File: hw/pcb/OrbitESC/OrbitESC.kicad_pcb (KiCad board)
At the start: 2 copper layers, 30 parts, among them J3 TermA, J4 TermB, J5 TermC, Q1 MCAC80N10Y, Q2 MCAC80N10Y, Q3 MCAC80N10Y, Q4 MCAC80N10Y, Q5 MCAC80N10Y, Q6 MCAC80N10Y, U1 MCP2551-I-SN, U2 AT25SF081-SSHD-X, U4 STM32F446ZCHx

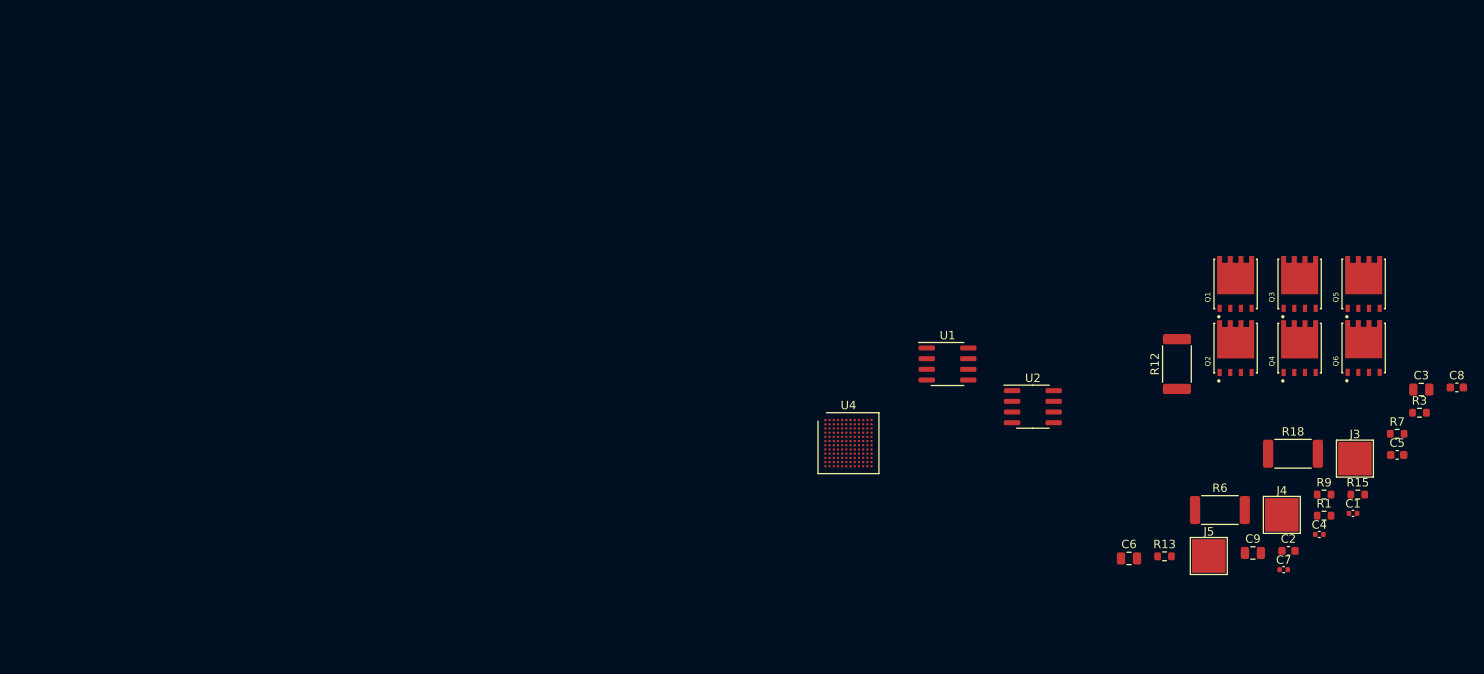
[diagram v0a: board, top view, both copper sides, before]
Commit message: Add power stage components
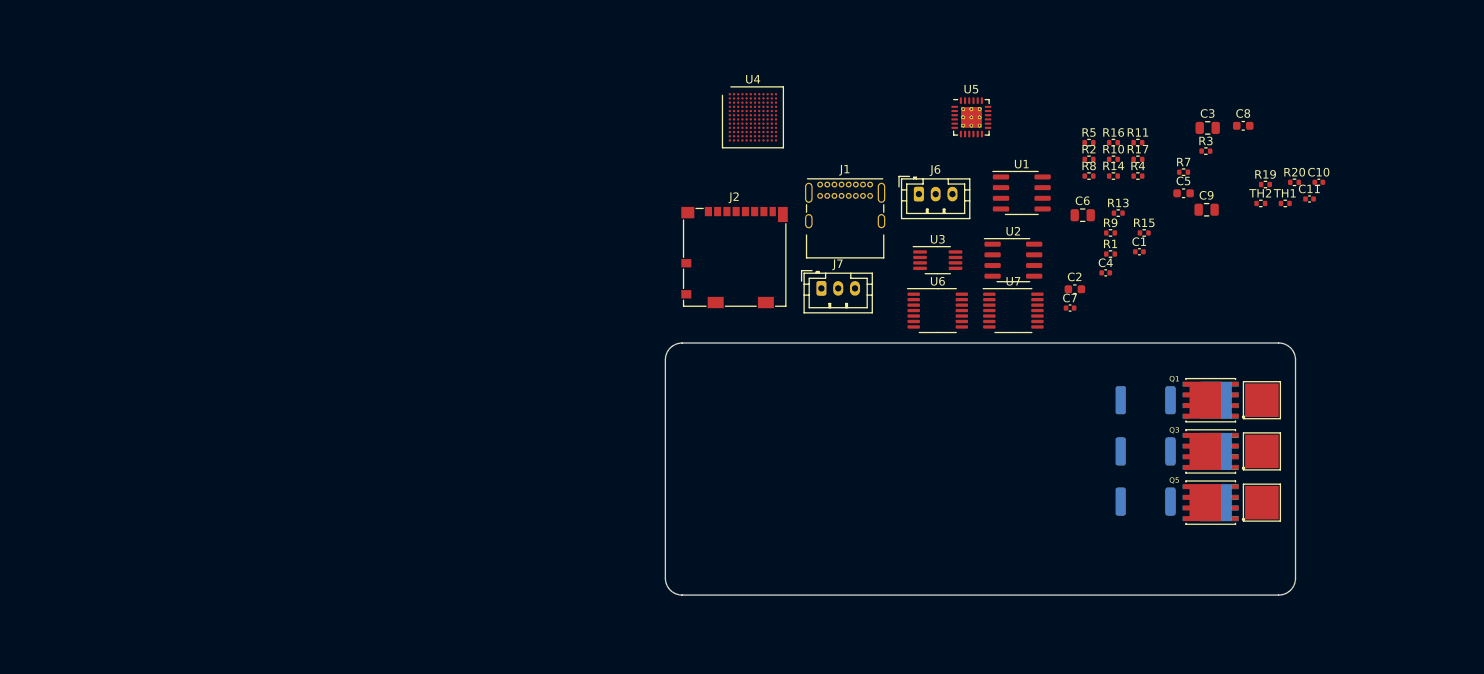
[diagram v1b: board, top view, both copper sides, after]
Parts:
- added C10: 1uF, Capacitor_SMD:C_0402_1005Metric, F.Cu at (181.3, 64.7)
- added C11: 1uF, Capacitor_SMD:C_0402_1005Metric, F.Cu at (180.2, 66.7)
- added J1: USB_C_Receptacle_USB2.0, Connector_USB:USB_C_Receptacle_GCT_USB4085, F.Cu at (122.0, 65.0)
- added J2: Micro_SD_Card_Det, Connector_Card:microSD_HC_Molex_104031-0811, F.Cu at (111.8, 73.7)
- added J6: CAN1, Connector_JST:JST_PH_B3B-PH-K_1x03_P2.00mm_Vertical, F.Cu at (133.8, 66.1)
- added J7: Serial1, Connector_JST:JST_PH_B3B-PH-K_1x03_P2.00mm_Vertical, F.Cu at (122.2, 77.4)
- added R10: 10, Resistor_SMD:R_0402_1005Metric, F.Cu at (156.9, 62.0)
- added R11: 39k, Resistor_SMD:R_0402_1005Metric, F.Cu at (159.8, 60.0)
- added R14: 10, Resistor_SMD:R_0402_1005Metric, F.Cu at (156.9, 64.0)
- added R16: 10, Resistor_SMD:R_0402_1005Metric, F.Cu at (156.9, 60.0)
- added R17: 39k, Resistor_SMD:R_0402_1005Metric, F.Cu at (159.8, 62.0)
- added R19: 1k, Resistor_SMD:R_0402_1005Metric, F.Cu at (175.0, 65.0)
- added R2: 10, Resistor_SMD:R_0402_1005Metric, F.Cu at (154.0, 62.0)
- added R20: 10k, Resistor_SMD:R_0402_1005Metric, F.Cu at (178.5, 64.7)
- added R4: 10, Resistor_SMD:R_0402_1005Metric, F.Cu at (159.8, 64.0)
- added R5: 39k, Resistor_SMD:R_0402_1005Metric, F.Cu at (154.0, 60.0)
- added R8: 10, Resistor_SMD:R_0402_1005Metric, F.Cu at (154.0, 64.0)
- added TH1: 10k NTC, Resistor_SMD:R_0402_1005Metric, F.Cu at (177.4, 67.2)
- added TH2: 10k NTC, Resistor_SMD:R_0402_1005Metric, F.Cu at (174.4, 67.2)
- added U3: 24LC128, Package_SO:MSOP-8_3x3mm_P0.65mm, F.Cu at (136.0, 74.0)
- added U5: DRV8300DRGER, Package_DFN_QFN:VQFN-24-1EP_4x4mm_P0.5mm_EP2.45x2.45mm_ThermalVias, F.Cu at (140.0, 57.0)
- added U6: TSV994, Package_SO:TSSOP-14_4.4x5mm_P0.65mm, F.Cu at (136.0, 80.0)
- added U7: TSV994, Package_SO:TSSOP-14_4.4x5mm_P0.65mm, F.Cu at (145.0, 80.0)
- Q2, Q4, Q6, R12, R18, R6: moved to B.Cu
- R1, R13: value 4.99k -> 1k; footprint Resistor_SMD:R_0603_1608Metric -> Resistor_SMD:R_0402_1005Metric
- R15, R3, R9: value 30k -> 10k; footprint Resistor_SMD:R_0603_1608Metric -> Resistor_SMD:R_0402_1005Metric
- R7: value 4.99k -> 10k; footprint Resistor_SMD:R_0603_1608Metric -> Resistor_SMD:R_0402_1005Metric
- moved C6 41.2 mm to (153.2, 68.7)
- moved C9 41.2 mm to (168.0, 68.0)
- moved R13 41.2 mm to (157.5, 68.4)
- moved U4 40.4 mm to (114.0, 57.0)
- moved C3 40.2 mm to (168.1, 58.3)
- moved C2 40.2 mm to (152.3, 77.5)
- moved C5 40.2 mm to (165.3, 66.0)
- moved R15 40.2 mm to (160.6, 70.8)
- moved R7 40.2 mm to (165.3, 63.5)
- moved C8 40.2 mm to (172.4, 58.0)
- moved R3 40.2 mm to (167.9, 61.0)
- moved C1 40.2 mm to (160.0, 73.0)
- moved C4 40.2 mm to (156.0, 75.5)
- moved C7 40.2 mm to (151.8, 79.7)
- moved R1 40.2 mm to (156.6, 73.3)
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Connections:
- C4 pad 1: /Outputs and Shunts/VA_FB -> /Outputs and Shunts/VB_FB
- C7 pad 1: /Outputs and Shunts/VA_FC -> /Outputs and Shunts/VC_FB
- R13 pad 2: /Outputs and Shunts/VA_FC -> /Outputs and Shunts/VB_FB
- R15 pad 1: /Outputs and Shunts/VA_FC -> /Outputs and Shunts/VB_FB
- R15 pad 2: /Outputs and Shunts/SH_C -> /Outputs and Shunts/SH_B
- R7 pad 1: GND -> /Outputs and Shunts/TempA
- R7 pad 2: /Outputs and Shunts/VA_FB -> GNDD
- R9 pad 1: /Outputs and Shunts/VA_FB -> /Outputs and Shunts/TempB
- R9 pad 2: /Outputs and Shunts/SH_B -> GNDD
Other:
- board outline added: 75 x 30 mm
- copper layers 2 -> 4

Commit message: Initial planning of MCU connections
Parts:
- added C12: 100nF, Capacitor_SMD:C_0402_1005Metric, F.Cu at (98.0, 71.0)
- added C13: 100nF, Capacitor_SMD:C_0402_1005Metric, F.Cu at (95.1, 74.0)
- added C14: 2.2uF, Capacitor_SMD:C_0805_2012Metric, F.Cu at (82.7, 70.5)
- added C15: 100nF, Capacitor_SMD:C_0402_1005Metric, F.Cu at (90.6, 77.0)
- added C16: 2.2uF, Capacitor_SMD:C_0805_2012Metric, F.Cu at (87.2, 70.5)
- added C17: 100nF, Capacitor_SMD:C_0402_1005Metric, F.Cu at (99.5, 69.0)
- added C18: 10uF, Capacitor_SMD:C_0805_2012Metric, F.Cu at (91.6, 67.5)
- added C19: 2.2uF, Capacitor_SMD:C_0805_2012Metric, F.Cu at (82.7, 67.5)
- added C20: 2.2uF, Capacitor_SMD:C_0805_2012Metric, F.Cu at (82.7, 73.6)
- added C21: 2.2uF, Capacitor_SMD:C_0805_2012Metric, F.Cu at (87.2, 67.5)
- added C22: 100nF, Capacitor_SMD:C_0402_1005Metric, F.Cu at (95.3, 60.8)
- added C23: 10uF, Capacitor_SMD:C_0805_2012Metric, F.Cu at (90.6, 56.8)
- added C24: 100nF, Capacitor_SMD:C_0402_1005Metric, F.Cu at (98.3, 57.3)
- added C25: 10uF, Capacitor_SMD:C_0805_2012Metric, F.Cu at (95.9, 50.8)
- added C26: 10uF, Capacitor_SMD:C_0805_2012Metric, F.Cu at (95.9, 47.8)
- added C27: 2.2uF, Capacitor_SMD:C_0805_2012Metric, F.Cu at (87.6, 59.9)
- added C28: 100nF, Capacitor_SMD:C_0402_1005Metric, F.Cu at (104.6, 52.3)
- added C29: 2.2uF, Capacitor_SMD:C_0805_2012Metric, F.Cu at (100.3, 47.8)
- added D1: Blue LED, Diode_SMD:D_0603_1608Metric, F.Cu at (100.2, 50.6)
- added D2: 18v, Diode_SMD:D_SMA, F.Cu at (84.5, 48.6)
- added D3: Blue LED, Diode_SMD:D_0603_1608Metric, F.Cu at (91.9, 59.6)
- added D4: Blue LED, Diode_SMD:D_0603_1608Metric, F.Cu at (95.3, 53.6)
- added D5: Blue LED, Diode_SMD:D_0603_1608Metric, F.Cu at (115.3, 47.6)
- added FB1: FerriteBead_Small, Resistor_SMD:R_0603_1608Metric, F.Cu at (94.8, 56.5)
- added L1: 4.7uH, Inductor_SMD:L_Bourns-SRN6028, F.Cu at (84.4, 54.6)
- added Q7: 2N7002, Package_TO_SOT_SMD:SOT-23, F.Cu at (90.8, 53.1)
- added R21: 10k, Resistor_SMD:R_0402_1005Metric, F.Cu at (95.1, 72.0)
- added R22: 10k, Resistor_SMD:R_0402_1005Metric, F.Cu at (92.2, 74.0)
- added R23: 10k, Resistor_SMD:R_0402_1005Metric, F.Cu at (86.4, 73.0)
- added R24: 1.5k, Resistor_SMD:R_0402_1005Metric, F.Cu at (95.3, 67.0)
- added R25: 10k, Resistor_SMD:R_0402_1005Metric, F.Cu at (81.9, 76.1)
- added R26: 1k, Resistor_SMD:R_0402_1005Metric, F.Cu at (89.3, 73.0)
- added R27: 1k, Resistor_SMD:R_0402_1005Metric, F.Cu at (96.7, 69.0)
- added R28: 10k, Resistor_SMD:R_0402_1005Metric, F.Cu at (98.2, 67.0)
- added R29: 10k, Resistor_SMD:R_0402_1005Metric, F.Cu at (90.8, 70.0)
- added R30: 10k, Resistor_SMD:R_0402_1005Metric, F.Cu at (101.1, 67.0)
- added R31: 10k, Resistor_SMD:R_0402_1005Metric, F.Cu at (89.3, 75.0)
- added R32: 1k, Resistor_SMD:R_0402_1005Metric, F.Cu at (84.8, 77.0)
- added R33: 1k, Resistor_SMD:R_0402_1005Metric, F.Cu at (87.8, 77.0)
- added R34: 10k, Resistor_SMD:R_0402_1005Metric, F.Cu at (92.2, 72.0)
- added R35: 1k, Resistor_SMD:R_0402_1005Metric, F.Cu at (86.4, 75.0)
- added R36: 1k, Resistor_SMD:R_0402_1005Metric, F.Cu at (93.7, 70.0)
- added R37: 10k, Resistor_SMD:R_0402_1005Metric, F.Cu at (98.8, 53.3)
- added R38: 10k, Resistor_SMD:R_0402_1005Metric, F.Cu at (104.0, 47.3)
- added R39: 1k, Resistor_SMD:R_0402_1005Metric, F.Cu at (103.6, 50.3)
- added R40: 51k, Resistor_SMD:R_0402_1005Metric, F.Cu at (106.5, 49.3)
- added R41: 10k, Resistor_SMD:R_0402_1005Metric, F.Cu at (91.3, 61.9)
- added R42: 10, Resistor_SMD:R_0402_1005Metric, F.Cu at (101.7, 52.9)
- added R43: 1.5k, Resistor_SMD:R_0402_1005Metric, F.Cu at (106.9, 47.3)
- added R44: 10k, Resistor_SMD:R_0402_1005Metric, F.Cu at (95.3, 58.8)
- added R45: 200, Resistor_SMD:R_0402_1005Metric, F.Cu at (101.7, 54.9)
- added R46: 49.9, Resistor_SMD:R_0402_1005Metric, F.Cu at (98.8, 55.3)
- added R47: 200, Resistor_SMD:R_0402_1005Metric, F.Cu at (114.7, 49.9)
- added U8: AP2171W, Package_TO_SOT_SMD:SOT-23-5, F.Cu at (91.1, 48.5)
- added U9: AP2120, Package_TO_SOT_SMD:SOT-23, F.Cu at (82.9, 60.6)
- U7: value TSV994 -> AP62200Z6-7; footprint Package_SO:TSSOP-14_4.4x5mm_P0.65mm -> Package_TO_SOT_SMD:SOT-563
- moved J1 47.5 mm to (142.8, 107.7)
- moved J6 46.4 mm to (106.0, 103.3)
- moved U5 40.7 mm to (153.9, 95.3)
- moved J7 35.5 mm to (106.0, 108.9)
- moved J2 18.6 mm to (110.8, 92.2), turned to 90 degrees
- moved J3 3.91 mm to (175.5, 86.9)
- moved Q1 3.91 mm to (169.4, 86.9)
- moved Q2 3.91 mm to (169.4, 86.9)
- moved R6 3.91 mm to (161.7, 86.9)
- moved J4 3.91 mm to (175.5, 93.0)
- moved J5 3.91 mm to (175.5, 99.1)
- moved Q3 3.91 mm to (169.4, 93.0)
- moved Q4 3.91 mm to (169.4, 93.0)
- moved Q5 3.91 mm to (169.4, 99.1)
- moved Q6 3.91 mm to (169.4, 99.1)
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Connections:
- U5 pad 1: unconnected-(U5-Pad1) -> /Power Stage/AL
- U5 pad 10: unconnected-(U5-Pad10) -> /Outputs and Shunts/GDL_B
- U5 pad 11: unconnected-(U5-Pad11) -> /Outputs and Shunts/GDL_A
- U5 pad 12: unconnected-(U5-Pad12) -> /Outputs and Shunts/SH_C
- U5 pad 13: unconnected-(U5-Pad13) -> /Outputs and Shunts/GDH_C
- U5 pad 14: unconnected-(U5-Pad14) -> Net-(U5-Pad14)
- U5 pad 15: unconnected-(U5-Pad15) -> /Outputs and Shunts/SH_B
- U5 pad 16: unconnected-(U5-Pad16) -> /Outputs and Shunts/GDH_B
- U5 pad 17: unconnected-(U5-Pad17) -> Net-(U5-Pad17)
- U5 pad 18: unconnected-(U5-Pad18) -> /Outputs and Shunts/SH_A
- U5 pad 19: unconnected-(U5-Pad19) -> /Outputs and Shunts/GDH_A
- U5 pad 2: unconnected-(U5-Pad2) -> /Power Stage/BL
- U5 pad 20: unconnected-(U5-Pad20) -> Net-(U5-Pad20)
- U5 pad 22: unconnected-(U5-Pad22) -> /Power Stage/AH
- U5 pad 23: unconnected-(U5-Pad23) -> /Power Stage/BH
- U5 pad 24: unconnected-(U5-Pad24) -> /Power Stage/CH
- U5 pad 3: unconnected-(U5-Pad3) -> /Power Stage/CL
- U5 pad 4: unconnected-(U5-Pad4) -> VDC
- U5 pad 6: unconnected-(U5-Pad6) -> GND
- U5 pad 9: unconnected-(U5-Pad9) -> /Outputs and Shunts/GDL_C
- U6 pad 1: unconnected-(U6-Pad1) -> /Power Stage/IC
- U6 pad 10: unconnected-(U6-Pad10) -> Net-(U6-Pad10)
- U6 pad 11: unconnected-(U6-Pad11) -> GND
- U6 pad 12: unconnected-(U6-Pad12) -> Net-(U6-Pad12)
- U6 pad 13: unconnected-(U6-Pad13) -> Net-(U6-Pad14)
- U6 pad 14: unconnected-(U6-Pad14) -> Net-(U6-Pad14)
- U6 pad 2: unconnected-(U6-Pad2) -> Net-(U6-Pad2)
- U6 pad 3: unconnected-(U6-Pad3) -> Net-(U6-Pad3)
- U6 pad 4: unconnected-(U6-Pad4) -> +3.3VADC
- U6 pad 5: unconnected-(U6-Pad5) -> Net-(U6-Pad5)
- U6 pad 6: unconnected-(U6-Pad6) -> Net-(U6-Pad6)
- U6 pad 7: unconnected-(U6-Pad7) -> /Power Stage/IA
- U6 pad 8: unconnected-(U6-Pad8) -> /Power Stage/IB
- U6 pad 9: unconnected-(U6-Pad9) -> Net-(U6-Pad9)
- U7 pad 1: unconnected-(U7-Pad1) -> VDC
- U7 pad 2: unconnected-(U7-Pad2) -> Net-(C24-Pad1)
- U7 pad 3: unconnected-(U7-Pad3) -> GNDD
- U7 pad 4: unconnected-(U7-Pad4) -> Net-(C24-Pad2)
- U7 pad 5: unconnected-(U7-Pad5) -> Net-(R37-Pad2)
- U7 pad 6: unconnected-(U7-Pad6) -> Net-(R40-Pad2)
